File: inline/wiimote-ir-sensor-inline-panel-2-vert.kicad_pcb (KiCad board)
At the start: 2 copper layers, 13 x 45 mm, 76 parts, among them J1 Conn_01x04_Pin, U2 AP2112-3.3V, X1 SG3225CAN 24.0000M-TJGA3

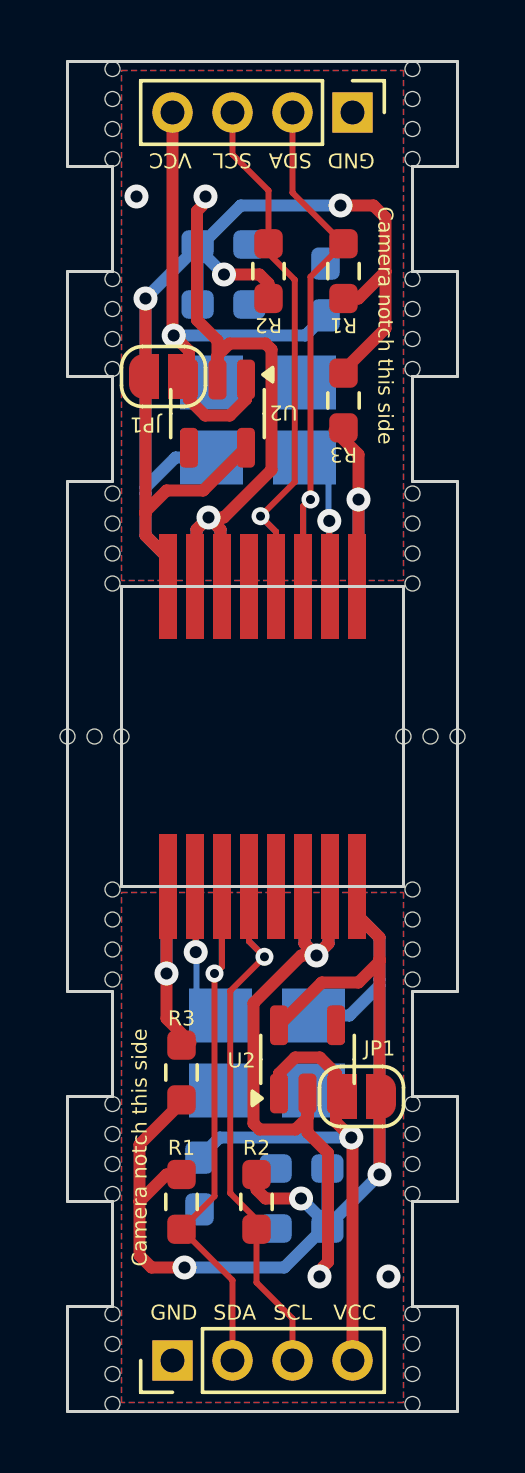
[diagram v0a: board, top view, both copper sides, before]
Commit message: Update inline board to allow wiring clock signal directly
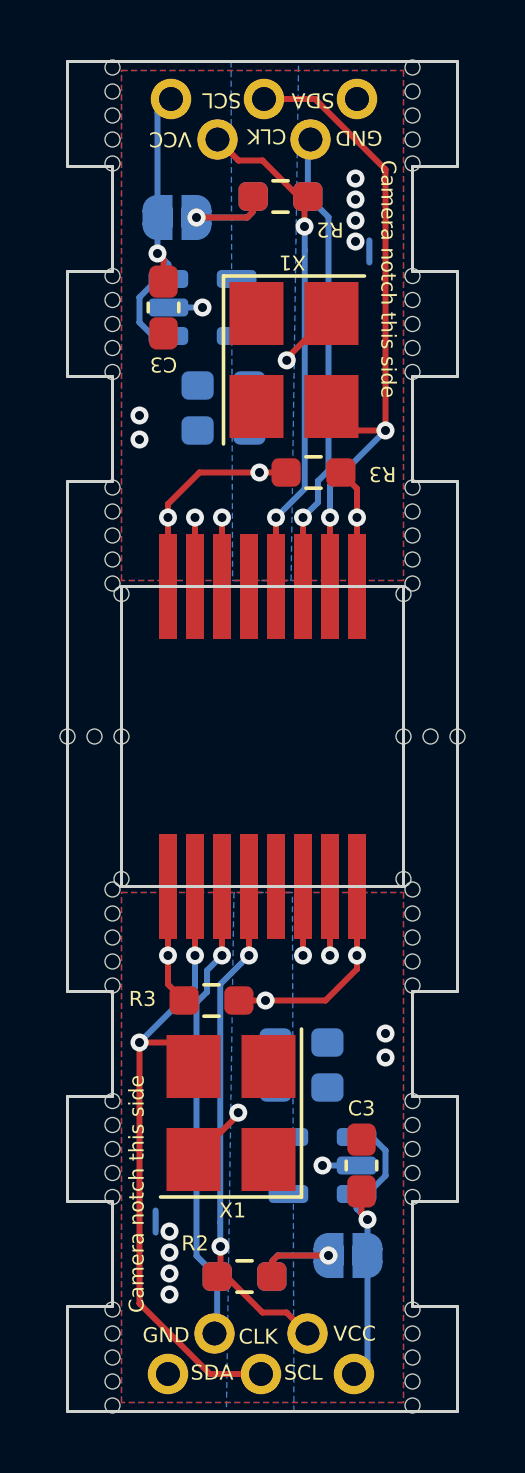
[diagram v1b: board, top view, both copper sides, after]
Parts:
- removed the C1 at (147.2, 26.1)
- removed the C1 at (149.8, 58.9)
- removed the C2 at (149.8, 56.9)
- removed the C2 at (147.2, 28.1)
- removed the C3 at (146.4, 57.4)
- removed the C3 at (150.6, 27.6)
- removed the J1 at (145.5, 63.3)
- removed the J1 at (151.5, 21.7)
- removed the JP1 at (151.8, 54.5)
- removed the JP1 at (145.2, 30.5)
- removed the R1 at (151.2, 27.0)
- removed the R1 at (145.8, 58.0)
- removed the R2 at (148.7, 27.0)
- removed the R2 at (148.3, 58.0)
- removed the R3 at (151.2, 31.3)
- removed the R3 at (145.8, 53.7)
- removed the REF** at (143.5, 22.2)
- removed the REF** at (153.5, 57.8)
- removed the REF** at (143.5, 57.8)
- removed the REF** at (153.5, 34.4)
- removed the REF** at (153.5, 56.8)
- removed the REF** at (143.5, 63.8)
- removed the REF** at (143.5, 27.2)
- removed the REF** at (143.5, 64.8)
- removed the REF** at (153.5, 27.2)
- removed the REF** at (153.5, 54.8)
- removed the REF** at (143.5, 54.8)
- removed the REF** at (143.5, 62.8)
- removed the REF** at (153.5, 23.2)
- removed the REF** at (153.5, 28.2)
- removed the REF** at (153.5, 64.8)
- removed the REF** at (153.5, 61.8)
- removed the REF** at (153.5, 50.6)
- removed the REF** at (143.5, 28.2)
- removed the REF** at (143.5, 34.4)
- removed the REF** at (143.5, 56.8)
- removed the REF** at (143.5, 30.2)
- removed the REF** at (143.5, 50.6)
- removed the REF** at (153.5, 55.8)
- removed the REF** at (143.5, 29.2)
- removed the REF** at (143.5, 48.6)
- removed the REF** at (153.5, 49.6)
- removed the REF** at (153.5, 21.2)
- removed the REF** at (153.5, 48.6)
- removed the REF** at (143.5, 20.2)
- removed the REF** at (143.5, 35.4)
- removed the REF** at (143.5, 49.6)
- removed the REF** at (153.5, 35.4)
- removed the REF** at (153.5, 22.2)
- removed the REF** at (153.5, 30.2)
- removed the REF** at (143.5, 21.2)
- removed the REF** at (143.5, 36.4)
- removed the REF** at (143.5, 55.8)
- removed the REF** at (153.5, 62.8)
- removed the REF** at (153.5, 29.2)
- removed the REF** at (153.5, 63.8)
- removed the REF** at (153.5, 20.2)
- removed the REF** at (153.5, 36.4)
- removed the REF** at (143.5, 23.2)
- removed the REF** at (143.5, 61.8)
- removed the U1 at (148.5, 45.0)
- removed the U1 at (148.5, 40.0)
- removed the U2 at (150.0, 53.3)
- removed the U2 at (147.0, 31.7)
- removed the X1 at (148.3, 31.9)
- removed the X1 at (148.7, 53.0)
- added C1: 0.1uF, Capacitor_SMD:C_0603_1608Metric_Pad1.08x0.95mm_HandSolder, B.Cu at (147.2, 32.3)
- added C1: 0.1uF, Capacitor_SMD:C_0603_1608Metric_Pad1.08x0.95mm_HandSolder, B.Cu at (149.8, 52.7)
- added C2: 1uF, Capacitor_SMD:C_0603_1608Metric_Pad1.08x0.95mm_HandSolder, B.Cu at (147.2, 30.8)
- added C2: 1uF, Capacitor_SMD:C_0603_1608Metric_Pad1.08x0.95mm_HandSolder, B.Cu at (149.8, 54.2)
- added C3: 1uF, Capacitor_SMD:C_0603_1608Metric_Pad1.08x0.95mm_HandSolder, F.Cu at (151.8, 56.8)
- added C3: 1uF, Capacitor_SMD:C_0603_1608Metric_Pad1.08x0.95mm_HandSolder, F.Cu at (145.2, 28.2)
- added J1: Conn_01x05_Pin, wiimote-ir-sensor:5Wires-staggered, F.Cu at (148.6, 21.9)
- added J1: Conn_01x05_Pin, wiimote-ir-sensor:5Wires-staggered, F.Cu at (148.4, 63.1)
- added JP1: SolderJumper_2_Open, Jumper:SolderJumper-2_P1.3mm_Open_RoundedPad1.0x1.5mm, B.Cu at (145.7, 25.2)
- added JP1: SolderJumper_2_Open, Jumper:SolderJumper-2_P1.3mm_Open_RoundedPad1.0x1.5mm, B.Cu at (151.3, 59.8)
- added R1: 2.7K, Resistor_SMD:R_0603_1608Metric_Pad0.98x0.95mm_HandSolder, B.Cu at (147.9, 60.5)
- added R1: 2.7K, Resistor_SMD:R_0603_1608Metric_Pad0.98x0.95mm_HandSolder, B.Cu at (149.1, 24.5)
- added R2: 2.7K, Resistor_SMD:R_0603_1608Metric_Pad0.98x0.95mm_HandSolder, F.Cu at (147.9, 60.5)
- added R2: 2.7K, Resistor_SMD:R_0603_1608Metric_Pad0.98x0.95mm_HandSolder, F.Cu at (149.1, 24.5)
- added R3: 33K, Resistor_SMD:R_0603_1608Metric_Pad0.98x0.95mm_HandSolder, F.Cu at (146.8, 51.3)
- added R3: 33K, Resistor_SMD:R_0603_1608Metric_Pad0.98x0.95mm_HandSolder, F.Cu at (150.2, 33.7)
- added REF**: NPTH-0.5mm, Panelization:NPTH-0.5mm, F.Cu at (143.5, 48.4)
- added REF**: NPTH-0.5mm, Panelization:NPTH-0.5mm, F.Cu at (143.5, 29.6)
- added REF**: NPTH-0.5mm, Panelization:NPTH-0.5mm, F.Cu at (153.5, 64.0)
- added REF**: NPTH-0.5mm, Panelization:NPTH-0.5mm, F.Cu at (153.5, 34.2)
- added REF**: NPTH-0.5mm, Panelization:NPTH-0.5mm, F.Cu at (143.5, 62.4)
- added REF**: NPTH-0.5mm, Panelization:NPTH-0.5mm, F.Cu at (143.5, 20.2)
- added REF**: NPTH-0.5mm, Panelization:NPTH-0.5mm, F.Cu at (143.5, 49.2)
- added REF**: NPTH-0.5mm, Panelization:NPTH-0.5mm, F.Cu at (153.5, 57.9)
- added REF**: NPTH-0.5mm, Panelization:NPTH-0.5mm, F.Cu at (143.5, 36.6)
- added REF**: NPTH-0.5mm, Panelization:NPTH-0.5mm, F.Cu at (153.5, 21.0)
- added REF**: NPTH-0.5mm, Panelization:NPTH-0.5mm, F.Cu at (143.5, 27.9)
- added REF**: NPTH-0.5mm, Panelization:NPTH-0.5mm, F.Cu at (153.5, 54.6)
- added REF**: NPTH-0.5mm, Panelization:NPTH-0.5mm, F.Cu at (143.5, 57.0)
- added REF**: NPTH-0.5mm, Panelization:NPTH-0.5mm, F.Cu at (153.2, 47.2)
- added REF**: NPTH-0.5mm, Panelization:NPTH-0.5mm, F.Cu at (143.5, 21.0)
- added REF**: NPTH-0.5mm, Panelization:NPTH-0.5mm, F.Cu at (153.5, 35.0)
- added REF**: NPTH-0.5mm, Panelization:NPTH-0.5mm, F.Cu at (143.5, 50.8)
- added REF**: NPTH-0.5mm, Panelization:NPTH-0.5mm, F.Cu at (143.5, 50.0)
- added REF**: NPTH-0.5mm, Panelization:NPTH-0.5mm, F.Cu at (153.5, 55.5)
- added REF**: NPTH-0.5mm, Panelization:NPTH-0.5mm, F.Cu at (143.5, 23.4)
- added REF**: NPTH-0.5mm, Panelization:NPTH-0.5mm, F.Cu at (153.5, 22.6)
- added REF**: NPTH-0.5mm, Panelization:NPTH-0.5mm, F.Cu at (143.5, 21.8)
- added REF**: NPTH-0.5mm, Panelization:NPTH-0.5mm, F.Cu at (153.2, 37.8)
- added REF**: NPTH-0.5mm, Panelization:NPTH-0.5mm, F.Cu at (153.5, 30.4)
- added REF**: NPTH-0.5mm, Panelization:NPTH-0.5mm, F.Cu at (143.8, 37.8)
- added REF**: NPTH-0.5mm, Panelization:NPTH-0.5mm, F.Cu at (143.5, 56.2)
- added REF**: NPTH-0.5mm, Panelization:NPTH-0.5mm, F.Cu at (153.5, 20.2)
- added REF**: NPTH-0.5mm, Panelization:NPTH-0.5mm, F.Cu at (153.5, 62.4)
- added REF**: NPTH-0.5mm, Panelization:NPTH-0.5mm, F.Cu at (143.8, 47.2)
- added REF**: NPTH-0.5mm, Panelization:NPTH-0.5mm, F.Cu at (153.5, 28.8)
- added REF**: NPTH-0.5mm, Panelization:NPTH-0.5mm, F.Cu at (143.5, 55.5)
- added REF**: NPTH-0.5mm, Panelization:NPTH-0.5mm, F.Cu at (143.5, 64.8)
- added REF**: NPTH-0.5mm, Panelization:NPTH-0.5mm, F.Cu at (153.5, 21.8)
- added REF**: NPTH-0.5mm, Panelization:NPTH-0.5mm, F.Cu at (143.5, 61.6)
- added REF**: NPTH-0.5mm, Panelization:NPTH-0.5mm, F.Cu at (153.5, 29.6)
- added REF**: NPTH-0.5mm, Panelization:NPTH-0.5mm, F.Cu at (143.5, 64.0)
- added REF**: NPTH-0.5mm, Panelization:NPTH-0.5mm, F.Cu at (143.5, 34.2)
- added REF**: NPTH-0.5mm, Panelization:NPTH-0.5mm, F.Cu at (153.5, 57.0)
- added REF**: NPTH-0.5mm, Panelization:NPTH-0.5mm, F.Cu at (153.5, 27.9)
- added REF**: NPTH-0.5mm, Panelization:NPTH-0.5mm, F.Cu at (143.5, 57.9)
- added REF**: NPTH-0.5mm, Panelization:NPTH-0.5mm, F.Cu at (153.5, 64.8)
- added REF**: NPTH-0.5mm, Panelization:NPTH-0.5mm, F.Cu at (143.5, 30.4)
- added REF**: NPTH-0.5mm, Panelization:NPTH-0.5mm, F.Cu at (153.5, 61.6)
- added REF**: NPTH-0.5mm, Panelization:NPTH-0.5mm, F.Cu at (143.5, 28.8)
- added REF**: NPTH-0.5mm, Panelization:NPTH-0.5mm, F.Cu at (153.5, 50.0)
- added REF**: NPTH-0.5mm, Panelization:NPTH-0.5mm, F.Cu at (143.5, 35.8)
- added REF**: NPTH-0.5mm, Panelization:NPTH-0.5mm, F.Cu at (153.5, 35.8)
- added REF**: NPTH-0.5mm, Panelization:NPTH-0.5mm, F.Cu at (153.5, 36.6)
- added REF**: NPTH-0.5mm, Panelization:NPTH-0.5mm, F.Cu at (153.5, 49.2)
- added REF**: NPTH-0.5mm, Panelization:NPTH-0.5mm, F.Cu at (153.5, 27.1)
- added REF**: NPTH-0.5mm, Panelization:NPTH-0.5mm, F.Cu at (143.5, 35.0)
- added REF**: NPTH-0.5mm, Panelization:NPTH-0.5mm, F.Cu at (143.5, 63.2)
- added REF**: NPTH-0.5mm, Panelization:NPTH-0.5mm, F.Cu at (153.5, 56.2)
- added REF**: NPTH-0.5mm, Panelization:NPTH-0.5mm, F.Cu at (153.5, 23.4)
- added REF**: NPTH-0.5mm, Panelization:NPTH-0.5mm, F.Cu at (153.5, 63.2)
- added REF**: NPTH-0.5mm, Panelization:NPTH-0.5mm, F.Cu at (143.5, 22.6)
- added REF**: NPTH-0.5mm, Panelization:NPTH-0.5mm, F.Cu at (143.5, 27.1)
- added REF**: NPTH-0.5mm, Panelization:NPTH-0.5mm, F.Cu at (143.5, 54.6)
- added REF**: NPTH-0.5mm, Panelization:NPTH-0.5mm, F.Cu at (153.5, 48.4)
- added REF**: NPTH-0.5mm, Panelization:NPTH-0.5mm, F.Cu at (153.5, 50.8)
- added U1: ~, wiimote-ir-sensor:wiimote-pixart-camera-inline_slim, B.Cu at (148.5, 45.0)
- added U1: ~, wiimote-ir-sensor:wiimote-pixart-camera-inline_slim, B.Cu at (148.5, 40.0)
- added U2: AP2112-3.3V, Package_TO_SOT_SMD:SOT-23-5, B.Cu at (146.5, 28.2)
- added U2: AP2112-3.3V, Package_TO_SOT_SMD:SOT-23-5, B.Cu at (150.5, 56.8)
- added X1: SG3225CAN 24.0000M-TJGA3, Oscillator:Oscillator_SMD_SeikoEpson_SG8002CE-4Pin_3.2x2.5mm_HandSoldering, F.Cu at (149.6, 29.9)
- added X1: SG3225CAN 24.0000M-TJGA3, Oscillator:Oscillator_SMD_SeikoEpson_SG8002CE-4Pin_3.2x2.5mm_HandSoldering, F.Cu at (147.4, 55.0)
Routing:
- net Board_1-+3.3V: track 46.7 -> 15.5 mm, vias 3 -> 4
- net Board_0-+3.3V: track 46.7 -> 15.5 mm, vias 3 -> 4
- net Board_1-/CLK: track 5.07 -> 24.1 mm, vias 1 -> 2
- net Board_0-/CLK: track 5.07 -> 24.1 mm, vias 1 -> 2
- net Board_0-GND: track 19.6 -> 11.1 mm, vias 3 -> 9
- net Board_1-GND: track 19.6 -> 11.1 mm, vias 3 -> 9
- net Board_0-VCC: track 18.1 -> 10.6 mm
- net Board_1-VCC: track 18.1 -> 10.6 mm
- net Board_0-/SCL: track 18.6 -> 19.5 mm, vias 1 -> 2
- net Board_1-/SCL: track 18.6 -> 19.5 mm, vias 1 -> 2
- net Board_1-Net-(U1-RESET): track 7.23 -> 6.32 mm
- net Board_0-Net-(U1-RESET): track 7.23 -> 6.32 mm
- net Board_1-/SDA: track 18.7 -> 17.9 mm
- net Board_0-/SDA: track 18.7 -> 17.9 mm
- added copper zone on B.Cu, net Board_0-+3.3V
- added copper zone on B.Cu, net Board_1-+3.3V
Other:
- board text added: "CLK"
